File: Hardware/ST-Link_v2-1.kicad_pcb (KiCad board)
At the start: 2 copper layers, 30.8 x 13.7 mm, 35 parts, among them J1 Conn_01x06, P1 USB_C_Plug_USB2.0, U1 STM32F103CBTx, U2 LP5907MFX-3.3, Y1 Crystal_Small

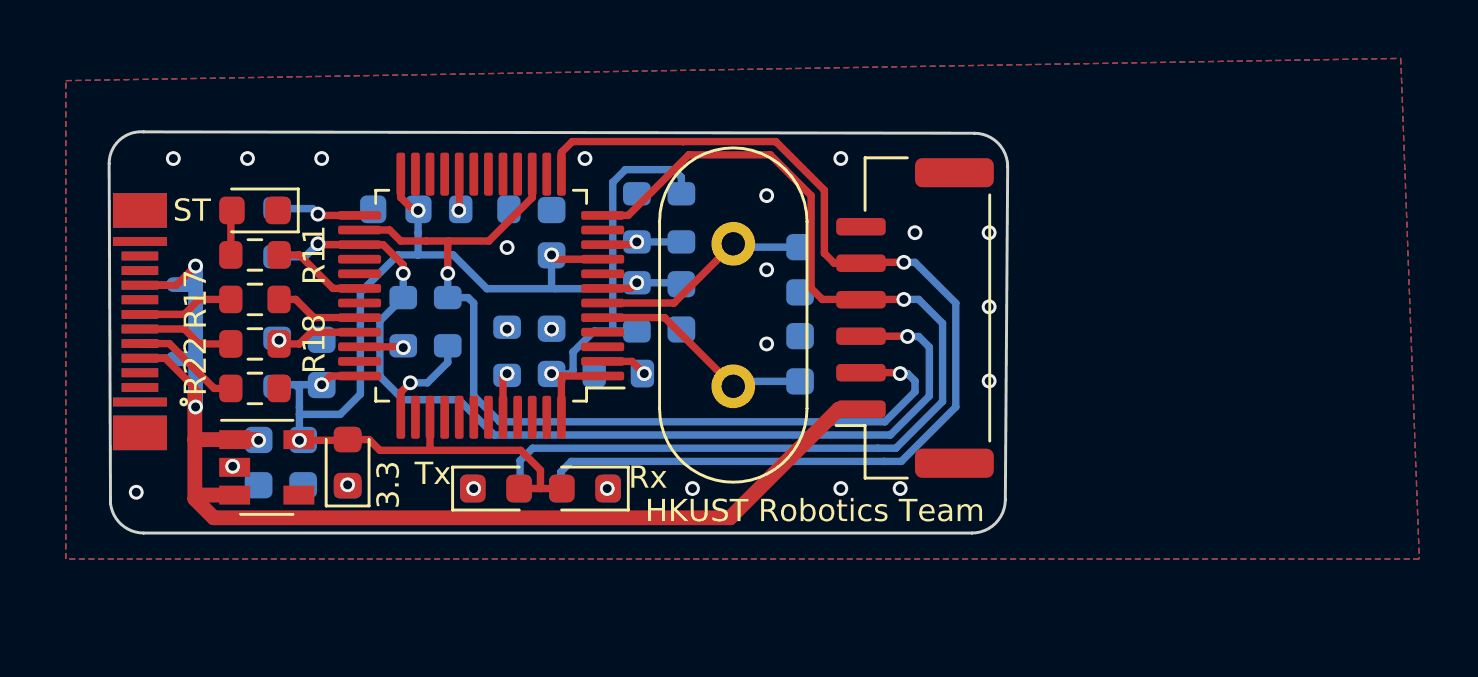
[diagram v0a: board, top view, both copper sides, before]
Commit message: 2.4 add esd protection
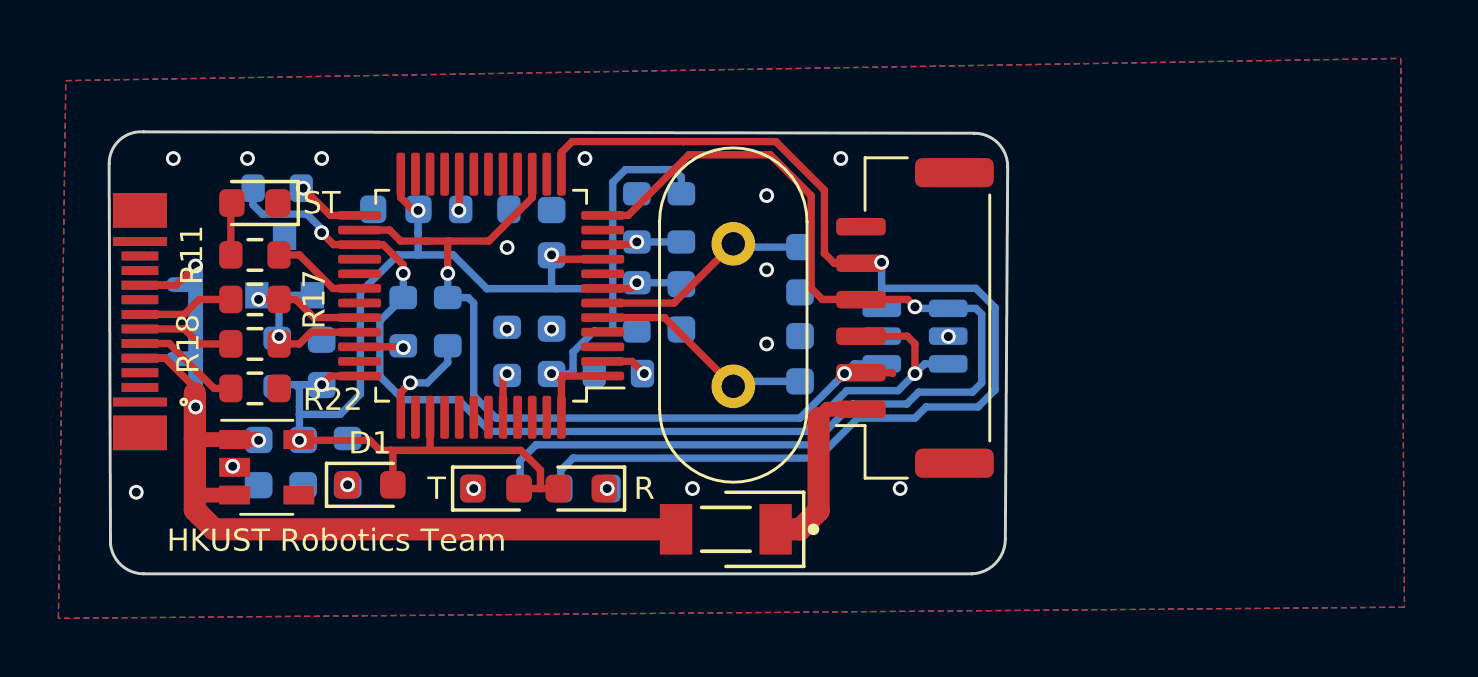
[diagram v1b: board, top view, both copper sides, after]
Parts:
- removed 3.3: 3.3V, HKUST_RT_BJT:LED_0603_1608Metric
- removed Rx: RX, HKUST_RT_BJT:LED_0603_1608Metric
- removed Tx: TX, HKUST_RT_BJT:LED_0603_1608Metric
- added D1: 3.3V, HKUST_RT_BJT:LED_0603_1608Metric, F.Cu at (149.0, 112.8)
- added D4: CESDBLC5V0AP, HKUST_RT_BJT:SOT-23, B.Cu at (146.1, 105.3)
- added D6: 1N4148, HKUST_RT_BJT:SOD-8OC, F.Cu at (161.2, 114.3)
- added R: RX, HKUST_RT_BJT:LED_0603_1608Metric, F.Cu at (156.2, 112.9)
- added T: TX, HKUST_RT_BJT:LED_0603_1608Metric, F.Cu at (153.3, 112.9)
- added U3: SRV05-4, HKUST_RT_BJT:SOT-23-6, B.Cu at (167.6, 107.7)
- moved R2 1.52 mm to (145.8, 102.6), turned to 180 degrees
- moved ST 0.25 mm to (145.0, 103.1)
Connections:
- J1 pad 1: +5V -> Net-(D6-Pad1)
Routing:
- net +5V: track 45.2 -> 38.2 mm
- net Net-(D6-Pad1): track 0.00 -> 6.49 mm
- net /RXD: track 36.6 -> 40.1 mm
- net /TXD: track 35.7 -> 38.2 mm
- net /D+: track 2.93 -> 5.28 mm
- net /JTMS: track 33.3 -> 35.0 mm
- net /JTCK: track 31.8 -> 30.3 mm
- net +3V3: track 53.7 -> 54.9 mm
- net /D-: track 3.02 -> 3.72 mm, vias 0 -> 1
- net Net-(R2-Pad1): track 2.92 -> 2.32 mm
- net GND: vias 20 -> 16
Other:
- board size 30.8 x 13.7 mm -> 30.8 x 15.1 mm
- board text added: "2022/4/11"
- board text added: "ST-Link-V2.1 V2.4"
- board text removed: "2022/1/23"
- board text removed: "ST-Link-V2.1 V2.3"

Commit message: 2.4 desgin rule check
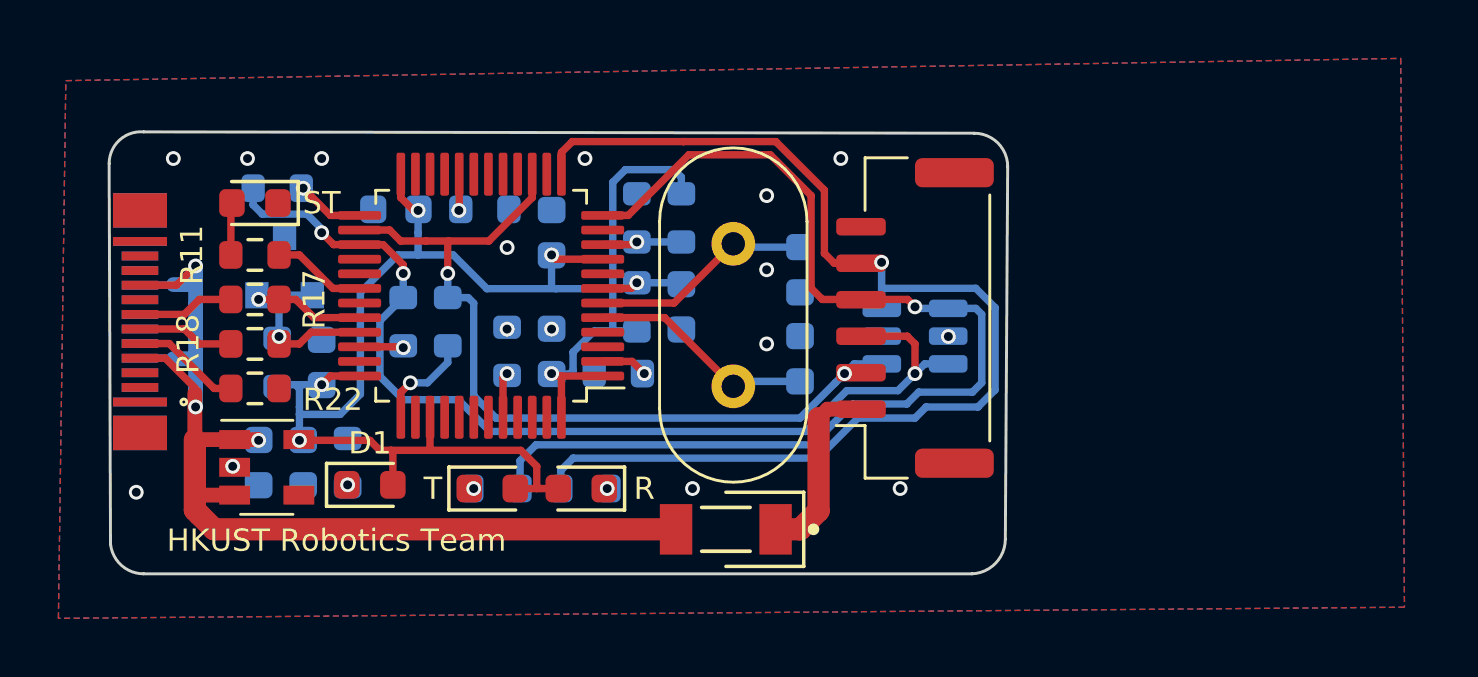
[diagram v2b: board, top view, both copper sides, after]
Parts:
- moved T 0.13 mm to (153.2, 112.9)
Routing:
- net /JTCK: track 30.3 -> 29.2 mm
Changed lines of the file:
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@@
   )
   (footprint "HKUST_RT_BJT:LED_0603_1608Metric" (layer "F.Cu")
-    (at 153.289 112.903)
+    (at 153.162 112.903)
     (descr "LED SMD 0603 (1608 Metric), square (rectangular) end terminal, IPC_7351 nominal, (Body size source: http://www.tortai-tech.com/upload/download/2011102023233369053.pdf), generated with kicad-footprint-generator")
     (tags "LED")
@@
     (property "Sheetname" "")
     (attr smd)
-    (fp_text reference "R14" (at 0 1.397 270) (layer "B.SilkS")
+    (fp_text reference "R14" (at 1.143 1.397 270) (layer "B.SilkS")
       (effects (font (size 0.762 0.762) (thickness 0.15)) (justify mirror))
     )
@@
     (property "Sheetname" "")
     (attr smd)
-    (fp_text reference "C8" (at 0 1.43 90) (layer "B.SilkS")
+    (fp_text reference "C8" (at 2.286 0 90) (layer "B.SilkS")
       (effects (font (size 0.762 0.762) (thickness 0.15)) (justify mirror))
     )
@@
     (property "Sheetname" "")
     (attr smd)
-    (fp_text reference "R3" (at 0 1.43 90) (layer "B.SilkS")
+    (fp_text reference "R3" (at 2.286 0 90) (layer "B.SilkS")
       (effects (font (size 0.762 0.762) (thickness 0.15)) (justify mirror))
     )
@@
     (property "Sheetname" "")
     (attr smd)
-    (fp_text reference "C9" (at 0 1.43 90) (layer "B.SilkS")
+    (fp_text reference "C9" (at 2.286 0 90) (layer "B.SilkS")
       (effects (font (size 0.762 0.762) (thickness 0.15)) (justify mirror))
     )
@@
   (segment (start 161.531 104.635) (end 161.417 104.521) (width 0.254) (layer "B.Cu") (net 4))
   (segment (start 163.703 104.635) (end 161.531 104.635) (width 0.254) (layer "B.Cu") (net 4))
+  (segment (start 154.0765 112.903) (end 154.686 112.903) (width 0.254) (layer "F.Cu") (net 5))
   (segment (start 154.813 112.903) (end 155.531 112.903) (width 0.254) (layer "F.Cu") (net 5))
   (segment (start 150.622 103.378) (end 150.46858 103.378) (width 0.254) (layer "F.Cu") (net 5))
@@
   (segment (start 155.531 110.4615) (end 155.531 109.049) (width 0.254) (layer "F.Cu") (net 5))
   (segment (start 148.6185 109.049) (end 147.618 109.049) (width 0.254) (layer "F.Cu") (net 5))
-  (segment (start 154.0765 112.903) (end 154.813 112.903) (width 0.254) (layer "F.Cu") (net 5))
   (segment (start 156.9435 105.049) (end 155.341 105.049) (width 0.254) (layer "F.Cu") (net 5))
-  (segment (start 151.09148 111.59448) (end 154.13948 111.59448) (width 0.254) (layer "F.Cu") (net 5))
+  (segment (start 154.13948 111.59448) (end 154.686 112.141) (width 0.254) (layer "F.Cu") (net 5))
   (segment (start 150.46858 103.378) (end 150.031 102.94042) (width 0.254) (layer "F.Cu") (net 5))
   (segment (start 155.341 105.049) (end 155.194 104.902) (width 0.254) (layer "F.Cu") (net 5))
@@
   (segment (start 146.558 111.252) (end 148.971 111.252) (width 0.254) (layer "F.Cu") (net 5))
   (segment (start 149.31348 111.59448) (end 149.69448 111.59448) (width 0.254) (layer "F.Cu") (net 5))
-  (segment (start 154.813 112.268) (end 154.813 112.903) (width 0.254) (layer "F.Cu") (net 5))
-  (segment (start 154.13948 111.59448) (end 154.813 112.268) (width 0.254) (layer "F.Cu") (net 5))
+  (segment (start 154.686 112.903) (end 154.813 112.903) (width 0.254) (layer "F.Cu") (net 5))
   (segment (start 151.031 110.4615) (end 151.031 111.534) (width 0.254) (layer "F.Cu") (net 5))
   (segment (start 151.031 111.534) (end 151.09148 111.59448) (width 0.254) (layer "F.Cu") (net 5))
   (segment (start 150.031 102.94042) (end 150.031 102.1365) (width 0.254) (layer "F.Cu") (net 5))
   (segment (start 155.277 109.049) (end 155.531 109.049) (width 0.254) (layer "F.Cu") (net 5))
+  (segment (start 151.09148 111.59448) (end 154.13948 111.59448) (width 0.254) (layer "F.Cu") (net 5))
+  (segment (start 154.686 112.141) (end 154.686 112.903) (width 0.254) (layer "F.Cu") (net 5))
   (via (at 155.194 104.902) (size 0.508) (drill 0.3048) (layers "F.Cu" "B.Cu") (net 5))
   (via (at 150.622 103.378) (size 0.508) (drill 0.3048) (layers "F.Cu" "B.Cu") (net 5))
@@
   (segment (start 144.339 113.1265) (end 143.1085 113.1265) (width 0.508) (layer "F.Cu") (net 6))
   (segment (start 141.96104 108.438) (end 142.9765 109.45346) (width 0.254) (layer "F.Cu") (net 6))
-  (segment (start 142.9765 111.2265) (end 142.9765 109.633066) (width 0.762) (layer "F.Cu") (net 6))
+  (segment (start 142.9765 111.2265) (end 142.9765 109.633066) (width 0.508) (layer "F.Cu") (net 6))
   (segment (start 143.129 113.147) (end 143.129 113.792) (width 0.254) (layer "F.Cu") (net 6))
   (segment (start 142.347 105.938) (end 143.002 105.283) (width 0.254) (layer "F.Cu") (net 6))
   (segment (start 142.9765 111.2265) (end 142.9765 113.6395) (width 0.762) (layer "F.Cu") (net 6))
-  (segment (start 142.9765 109.45346) (end 142.9765 109.633066) (width 0.254) (layer "F.Cu") (net 6))
   (segment (start 141.097 105.938) (end 142.347 105.938) (width 0.254) (layer "F.Cu") (net 6))
   (segment (start 144.339 111.2265) (end 145.1355 111.2265) (width 0.508) (layer "F.Cu") (net 6))
@@
   (segment (start 143.002 108.458) (end 143.002 106.593) (width 0.508) (layer "B.Cu") (net 6))
   (segment (start 141.097 108.438) (end 142.22 108.438) (width 0.254) (layer "B.Cu") (net 6))
-  (segment (start 142.982 108.438) (end 143.002 108.458) (width 0.254) (layer "B.Cu") (net 6))
   (segment (start 143.002 105.918) (end 143.002 106.593) (width 0.508) (layer "B.Cu") (net 6))
   (segment (start 141.097 105.938) (end 142.22 105.938) (width 0.254) (layer "B.Cu") (net 6))
@@
   (segment (start 149.64696 104.049) (end 150.023308 104.425349) (width 0.254) (layer "F.Cu") (net 14))
   (segment (start 148.6185 104.049) (end 149.64696 104.049) (width 0.254) (layer "F.Cu") (net 14))
-  (segment (start 166.848 108.936) (end 165.79 108.936) (width 0.254) (layer "F.Cu") (net 14))
-  (segment (start 166.878 108.966) (end 166.848 108.936) (width 0.254) (layer "F.Cu") (net 14))
   (segment (start 165.257 108.936) (end 165.79 108.936) (width 0.254) (layer "F.Cu") (net 14))
   (segment (start 151.638 104.456698) (end 151.669349 104.425349) (width 0.254) (layer "F.Cu") (net 14))

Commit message: v2.5
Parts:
- removed R: RX, HKUST_RT_BJT:LED_0603_1608Metric
- removed ST: LED_Small, HKUST_RT_BJT:LED_0603_1608Metric
- removed T: TX, HKUST_RT_BJT:LED_0603_1608Metric
- added D2: TX, HKUST_RT_BJT:LED_0603_1608Metric, F.Cu at (153.2, 112.9)
- added D3: RX, HKUST_RT_BJT:LED_0603_1608Metric, F.Cu at (156.3, 112.9)
- added D5: LED_Small, HKUST_RT_BJT:LED_0603_1608Metric, F.Cu at (145.0, 103.4)
- C2, C3: value 22pF -> 20pF; moved to F.Cu
- Y1: value Crystal_Small -> 8MHz; footprint HKUST_RT_RCL:Crystal_HC49-4H_Vertical -> HKUST_RT_RCL:Crystal_SMD_3225-4Pin_3.2x2.5mm
- moved C3 3.42 mm to (160.7, 103.8), turned to 180 degrees
- moved C2 3.12 mm to (160.9, 109.7), turned to 0 degrees
- moved Y1 2.25 mm to (160.8, 106.7)
- moved U3 1.83 mm to (165.8, 107.4)
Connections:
- C2 pad 1: Net-(C2-Pad1) -> GND
- C2 pad 2: GND -> Net-(U1-Pad5)
- C3 pad 1: Net-(C3-Pad1) -> GND
- C3 pad 2: GND -> Net-(U1-Pad6)
- U1 pad 5: Net-(C2-Pad1) -> Net-(U1-Pad5)
- U1 pad 6: Net-(C3-Pad1) -> Net-(U1-Pad6)
- Y1 pad 1: Net-(C3-Pad1) -> Net-(U1-Pad6)
- Y1 pad 2: Net-(C2-Pad1) -> GND
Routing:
- net Net-(C2-Pad1): track 7.80 -> 0.00 mm
- net Net-(U1-Pad5): track 0.00 -> 7.71 mm
- net Net-(C3-Pad1): track 7.65 -> 0.00 mm
- net Net-(U1-Pad6): track 0.00 -> 5.21 mm
- net GND: track 0.00 -> 2.16 mm, vias 16 -> 24
- net /JTMS: track 35.0 -> 36.6 mm
- net /RXD: track 40.1 -> 40.8 mm
- net /TXD: track 38.2 -> 37.6 mm
- net /JTCK: track 29.2 -> 29.8 mm
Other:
- board text added: "2022/5/9"
- board text added: "Rx"
- board text added: "ST"
- board text added: "ST-Link-V2.1 V2.5"
- board text added: "Tx"
- board text removed: "2022/4/11"
- board text removed: "ST-Link-V2.1 V2.4"
